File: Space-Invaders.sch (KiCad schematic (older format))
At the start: 73 parts, among them Q1 BS170, Q2 BS170, Q3 BS170, Q4 BS170, U1 LM556, U2 LM3900, U3 4070, U4 CD4006

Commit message: annotate
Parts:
- gave numbers to parts that had none: 9
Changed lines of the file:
@@
 PLAYER\nKILLED
 $Comp
-L Xenir:LM358 U?
+L Xenir:LM358 U5
 U 1 1 6344A0F4
 P 6350 7900
-F 0 "U?" H 6300 7900 70  0000 C CNN
+F 0 "U5" H 6300 7900 70  0000 C CNN
 F 1 "LM358" H 6400 7700 70  0000 C CNN
 F 2 "" H 6300 7850 50  0001 C CNN
@@
 $EndComp
 $Comp
-L Amplifier_Audio:LM386 U?
+L Amplifier_Audio:LM386 U6
 U 1 1 6344BBDF
 P 7850 8000
-F 0 "U?" H 7900 8150 50  0000 L CNN
+F 0 "U6" H 7900 8150 50  0000 L CNN
 F 1 "LM386" H 7400 7850 50  0000 L CNN
 F 2 "" H 7950 8100 50  0001 C CNN
@@
 $EndComp
 $Comp
-L Xenir:Trimpot VR?
+L Xenir:Trimpot VR1
 U 1 1 6344D0C5
 P 6800 8100
-F 0 "VR?" V 6846 8018 50  0000 L CNN
+F 0 "VR1" V 6846 8018 50  0000 L CNN
 F 1 "50k" V 6755 8018 50  0000 L CNN
 F 2 "" H 6650 7800 50  0001 C CNN
@@
 Connection ~ 6650 7900
 $Comp
-L power:GND #PWR?
+L power:GND #PWR028
 U 1 1 634554E3
 P 6950 8300
-F 0 "#PWR?" H 6950 8050 50  0001 C CNN
+F 0 "#PWR028" H 6950 8050 50  0001 C CNN
 F 1 "GND" H 6955 8127 50  0000 C CNN
 F 2 "" H 6950 8300 50  0001 C CNN
@@
 $EndComp
 $Comp
-L Xenir:Cap_Polarized C?
+L Xenir:Cap_Polarized C11
 U 1 1 6346C243
 P 5900 7900
-F 0 "C?" V 5871 7918 28  0000 L CNN
+F 0 "C11" V 5871 7918 28  0000 L CNN
 F 1 "10uF" V 5928 7918 28  0000 L CNN
 F 2 "" H 5900 7950 50  0001 C CNN
@@
 $EndComp
 $Comp
-L power:GND #PWR?
+L power:GND #PWR029
 U 1 1 6347CD19
 P 7550 7900
-F 0 "#PWR?" H 7550 7650 50  0001 C CNN
+F 0 "#PWR029" H 7550 7650 50  0001 C CNN
 F 1 "GND" H 7400 7850 50  0000 C CNN
 F 2 "" H 7550 7900 50  0001 C CNN
@@
 	7150 8100 7550 8100
 $Comp
-L power:+12V #PWR?
+L power:+12V #PWR031
 U 1 1 634801A1
 P 7750 7700
-F 0 "#PWR?" H 7750 7550 50  0001 C CNN
+F 0 "#PWR031" H 7750 7550 50  0001 C CNN
 F 1 "+12V" H 7765 7873 50  0000 C CNN
 F 2 "" H 7750 7700 50  0001 C CNN
@@
 $EndComp
 $Comp
-L Xenir:Cap_Polarized C?
+L Xenir:Cap_Polarized C12
 U 1 1 63480FE9
 P 7950 8450
-F 0 "C?" V 7921 8468 28  0000 L CNN
+F 0 "C12" V 7921 8468 28  0000 L CNN
 F 1 "10uF" V 7978 8468 28  0000 L CNN
 F 2 "" H 7950 8500 50  0001 C CNN
@@
 	8100 8600 7850 8600
 $Comp
-L power:GND #PWR?
+L power:GND #PWR030
 U 1 1 6348A1EE
 P 7650 8300
-F 0 "#PWR?" H 7650 8050 50  0001 C CNN
+F 0 "#PWR030" H 7650 8050 50  0001 C CNN
 F 1 "GND" H 7500 8250 50  0000 C CNN
 F 2 "" H 7650 8300 50  0001 C CNN
@@
 	7750 8300 7650 8300
 $Comp
-L Xenir:Capacitor C?
+L Xenir:Capacitor C13
 U 1 1 63490CCB
 P 8450 8150
-F 0 "C?" H 8450 8351 28  0000 C CNN
+F 0 "C13" H 8450 8351 28  0000 C CNN
 F 1 "470nF" H 8450 8294 28  0000 C CNN
 F 2 "" H 8450 8000 50  0001 C CNN
@@
 $EndComp
 $Comp
-L Xenir:Resistor R?
+L Xenir:Resistor R41
 U 1 1 63493C7B
 P 8450 8500
-F 0 "R?" V 8479 8432 28  0000 R CNN
+F 0 "R41" V 8479 8432 28  0000 R CNN
 F 1 "10" V 8422 8432 28  0000 R CNN
 F 2 "" H 8450 8400 50  0001 C CNN
@@
 $EndComp
 $Comp
-L power:GND #PWR?
+L power:GND #PWR032
 U 1 1 63496BAC
 P 8450 8700
-F 0 "#PWR?" H 8450 8450 50  0001 C CNN
+F 0 "#PWR032" H 8450 8450 50  0001 C CNN
 F 1 "GND" H 8300 8650 50  0000 C CNN
 F 2 "" H 8450 8700 50  0001 C CNN
@@
 $EndComp
 $Comp
-L Xenir:Cap_Polarized C?
+L Xenir:Cap_Polarized C14
 U 1 1 634978B4
 P 8850 7900
-F 0 "C?" V 8821 7918 28  0000 L CNN
+F 0 "C14" V 8821 7918 28  0000 L CNN
 F 1 "47uF" V 8878 7918 28  0000 L CNN
 F 2 "" H 8850 7950 50  0001 C CNN
@@
 	8450 8000 8700 8000
 $Comp
-L Device:Speaker LS?
+L Device:Speaker LS1
 U 1 1 6349B96A
 P 9200 8000
-F 0 "LS?" H 9370 7996 50  0000 L CNN
+F 0 "LS1" H 9370 7996 50  0000 L CNN
 F 1 "Speaker" H 9370 7905 50  0000 L CNN
 F 2 "" H 9200 7800 50  0001 C CNN
@@
 $EndComp
 $Comp
-L power:GND #PWR?
+L power:GND #PWR033
 U 1 1 6349BEC1
 P 9000 8100
-F 0 "#PWR?" H 9000 7850 50  0001 C CNN
+F 0 "#PWR033" H 9000 7850 50  0001 C CNN
 F 1 "GND" H 8850 8050 50  0000 C CNN
 F 2 "" H 9000 8100 50  0001 C CNN

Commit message: gg
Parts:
- removed unit 1 of U2
- added U?: LM3900, symbol Xenir:LM3900
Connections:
- net at R28.2, R30.1: now also U?.1 (+)
- net at D5.1 (K), R30.2, R31.2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: now also U?.5
- net at R27.2, R29.2: now also U?.6 (-)
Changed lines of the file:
@@
-$Comp
-L Xenir:LM3900 U2
-U 1 1 634082C5
-P 8250 5000
-F 0 "U2" H 8250 5000 50  0000 C CNN
-F 1 "LM3900" H 8350 4850 50  0000 C CNN
-F 2 "" H 8130 5050 50  0001 C CNN
-F 3 "" H 8130 5050 50  0001 C CNN
-	1    8250 5000
-	1    0    0    -1
-$EndComp
 $Comp
 L Xenir:LM3900 U2
@@
 Text Notes 3800 2600 0    118  ~ 0
 FET DRIVER CIRCUIT\n(not original)
+$Comp
+L Xenir:LM3900 U?
+U 1 1 6341538E
+P 8250 5000
+F 0 "U?" H 8250 5367 50  0000 C CNN
+F 1 "LM3900" H 8250 5276 50  0000 C CNN
+F 2 "" H 8130 5050 50  0001 C CNN
+F 3 "" H 8130 5050 50  0001 C CNN
+	1    8250 5000
+	1    0    0    -1
+$EndComp
 $EndSCHEMATC

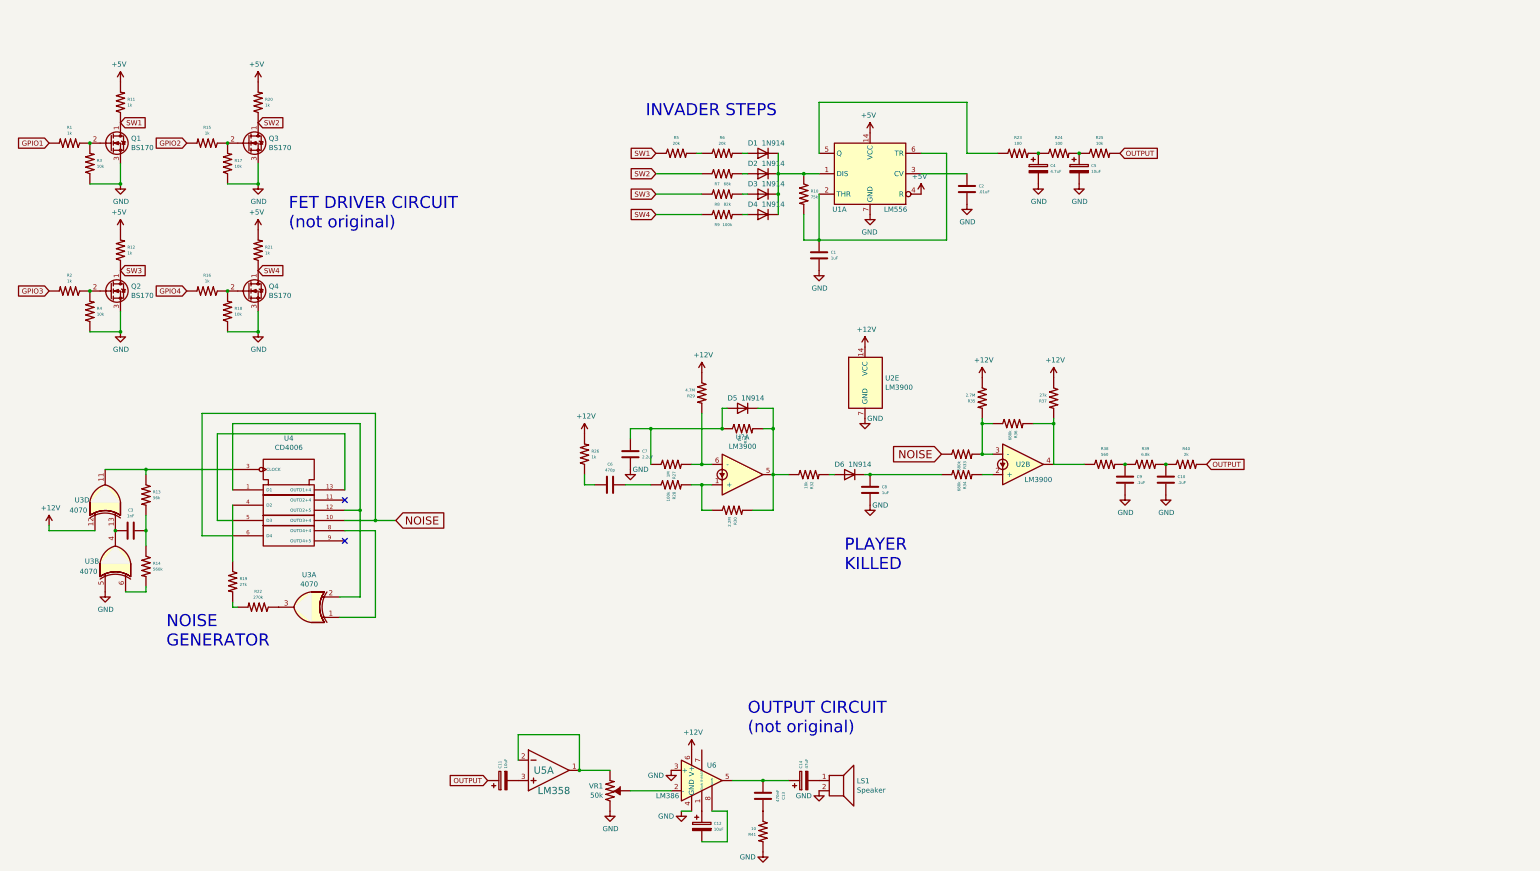
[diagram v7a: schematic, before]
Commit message: added sn76477
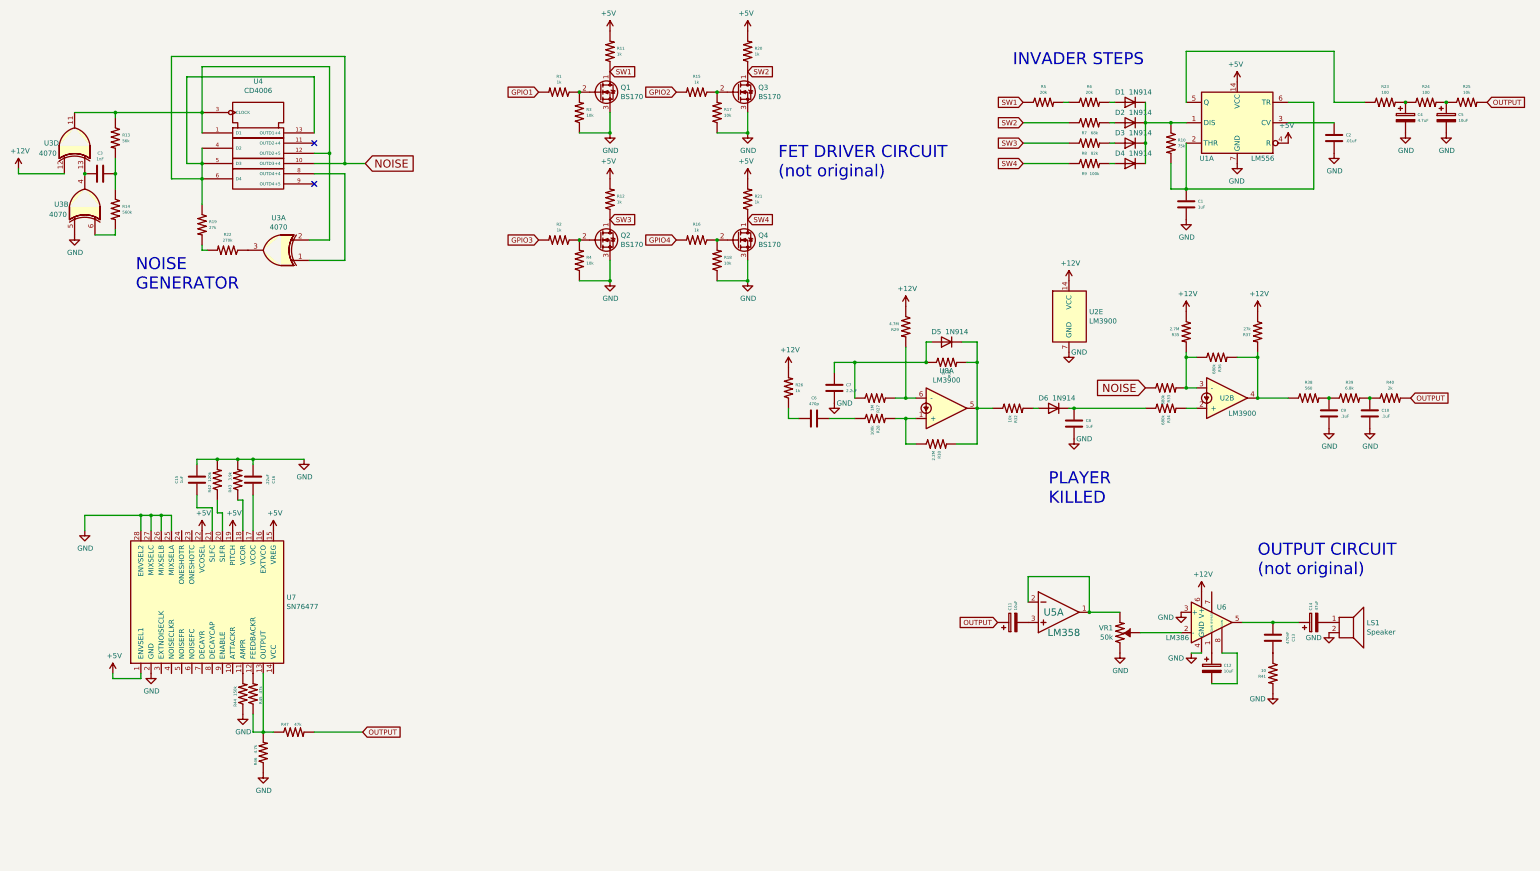
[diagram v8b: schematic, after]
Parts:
- added C15: 1uF, symbol Xenir:Capacitor
- added C16: .22uF, symbol Xenir:Capacitor
- added R42: 120k, symbol Xenir:Resistor
- added R43: 3.9k, symbol Xenir:Resistor
- added R44: 150k, symbol Xenir:Resistor
- added R45, R47: 47k, symbol Xenir:Resistor
- added R46: 4.7k, symbol Xenir:Resistor
- added U7: SN76477, symbol Xenir:SN76477
- gave numbers to parts that had none: 1
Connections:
- net +5V: now also U7.1 (ENVSEL1), U7.15 (VREG), U7.19 (PITCH), U7.22 (VCOSEL)
- net GND: now also C15.1, C16.1, R42.2, R43.2, R44.1, R46.1, U7.2 (GND), U7.25 (MIXSELA), U7.26 (MIXSELB), U7.27 (MIXSELC), U7.28 (ENVSEL2)
- net NOISE: now also R19.1, U4.13 (OUTD1+4), U4.4 (D2), U4.5 (D3)
- net OUTPUT: now also R47.2
- net at R13.1, U3.11, U4.3 (CLOCK): now also U3.2, U4.1 (D1), U4.12 (OUTD2+5)
- new net: R44.2, U7.11 (AMPR)
- new net: R45.2, U7.12 (FEEDBACKR)
- new net: R45.1, R46.2, R47.1, U7.13 (OUTPUT)
- new net: C16.2, U7.17 (VCOC)
- new net: R43.1, U7.18 (VCOR)
- new net: R42.1, U7.20 (SLFR)
- new net: C15.2, U7.21 (SLFC)
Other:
- moved on the sheet: C1, C10, C11, C12, C13, C14, C2, C3, C4, C5, C6, C7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
